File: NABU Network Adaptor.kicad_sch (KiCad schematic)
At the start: 19 parts, among them J1 DIN-5_180degree, J3 RF Module, J5 LEDs, U1 SN74LS164N, U10 UA9638CP, U11 UA9637ATC, U13 SN74LS164N, U19 LM339N, U20 SN74LS164N, U21 SN74LS86N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

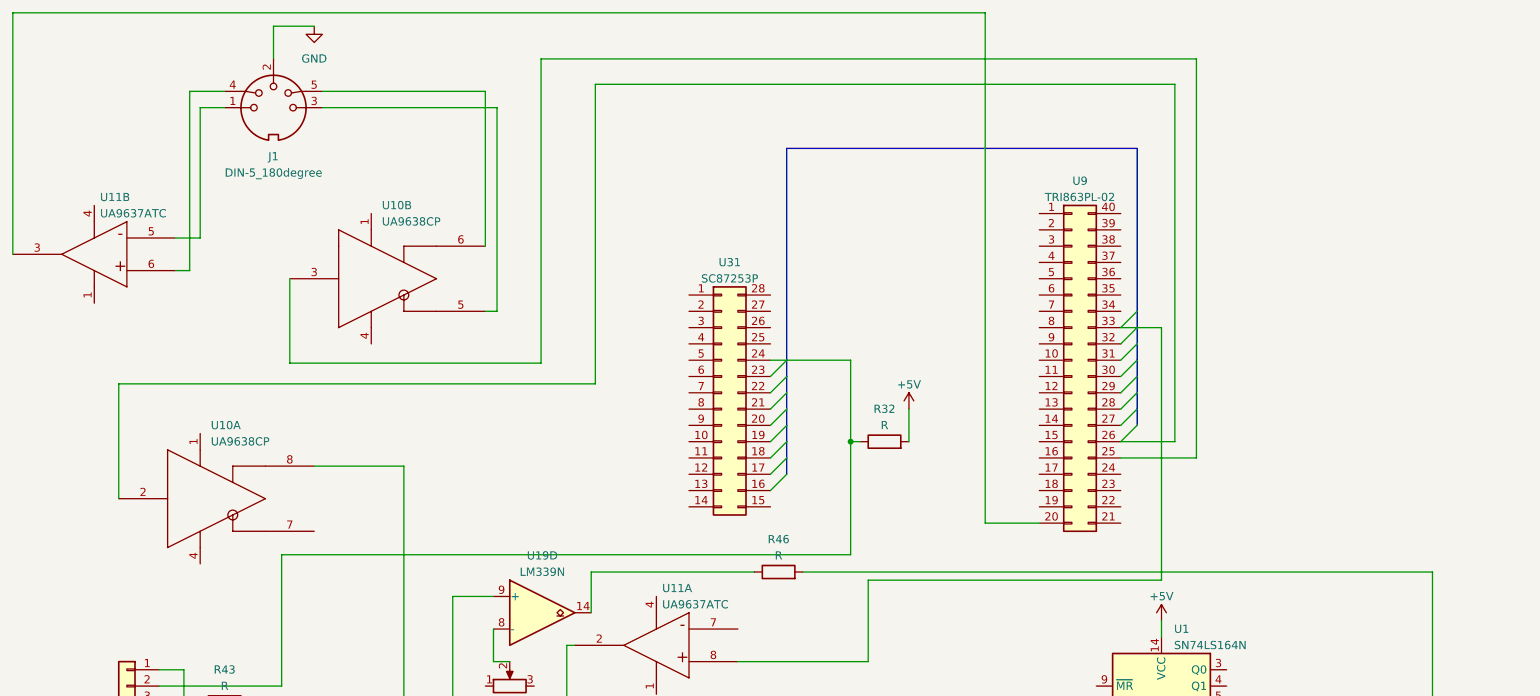
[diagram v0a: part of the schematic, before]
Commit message: Add U8
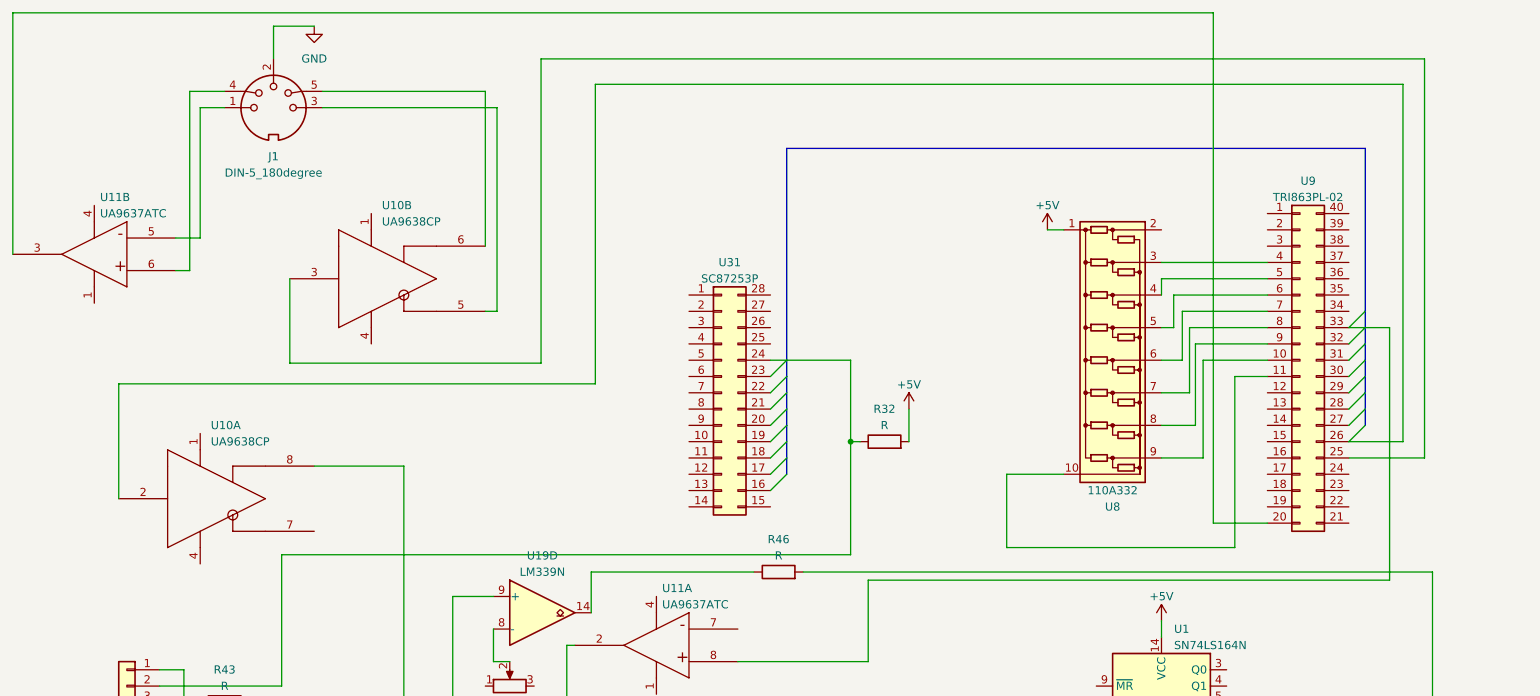
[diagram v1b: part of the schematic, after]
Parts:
- added U8: 110A332, Resistor_THT:R_Array_SIP10, symbol Device:R_Network_Dividers_x08_SIP
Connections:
- net +5V: now also U8.1 (COM1)
- net at U9.10 (Pin_10): now also U8.9 (R8)
- net at U9.11 (Pin_11): now also U8.10 (COM2)
- net at U9.4 (Pin_4): now also U8.3 (R2)
- net at U9.5 (Pin_5): now also U8.4 (R3)
- net at U9.6 (Pin_6): now also U8.5 (R4)
- net at U9.7 (Pin_7): now also U8.6 (R5)
- net at U9.8 (Pin_8): now also U8.7 (R6)
- net at U9.9 (Pin_9): now also U8.8 (R7)
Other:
- moved on the sheet: U9

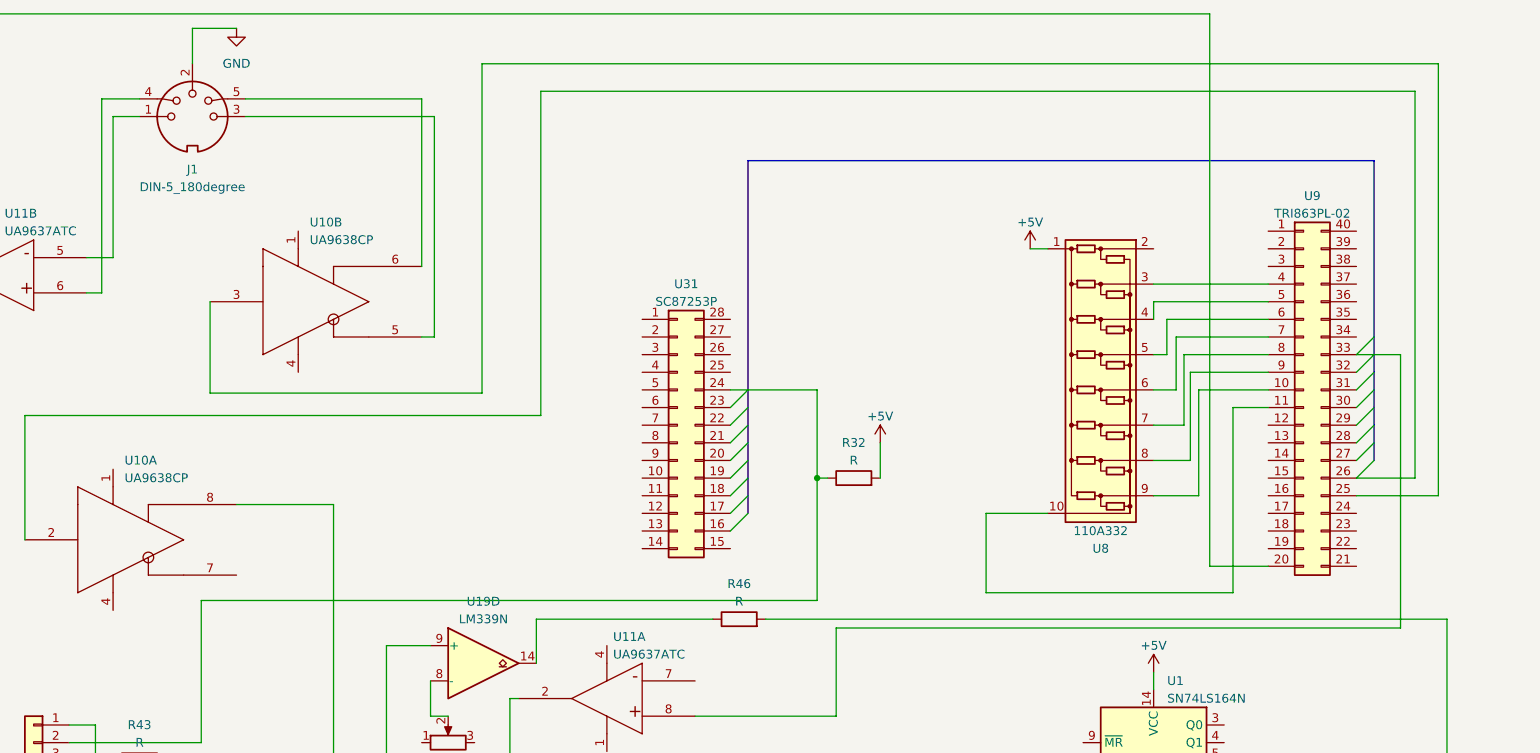
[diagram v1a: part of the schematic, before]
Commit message: Fix U10/U11 to U9 connections
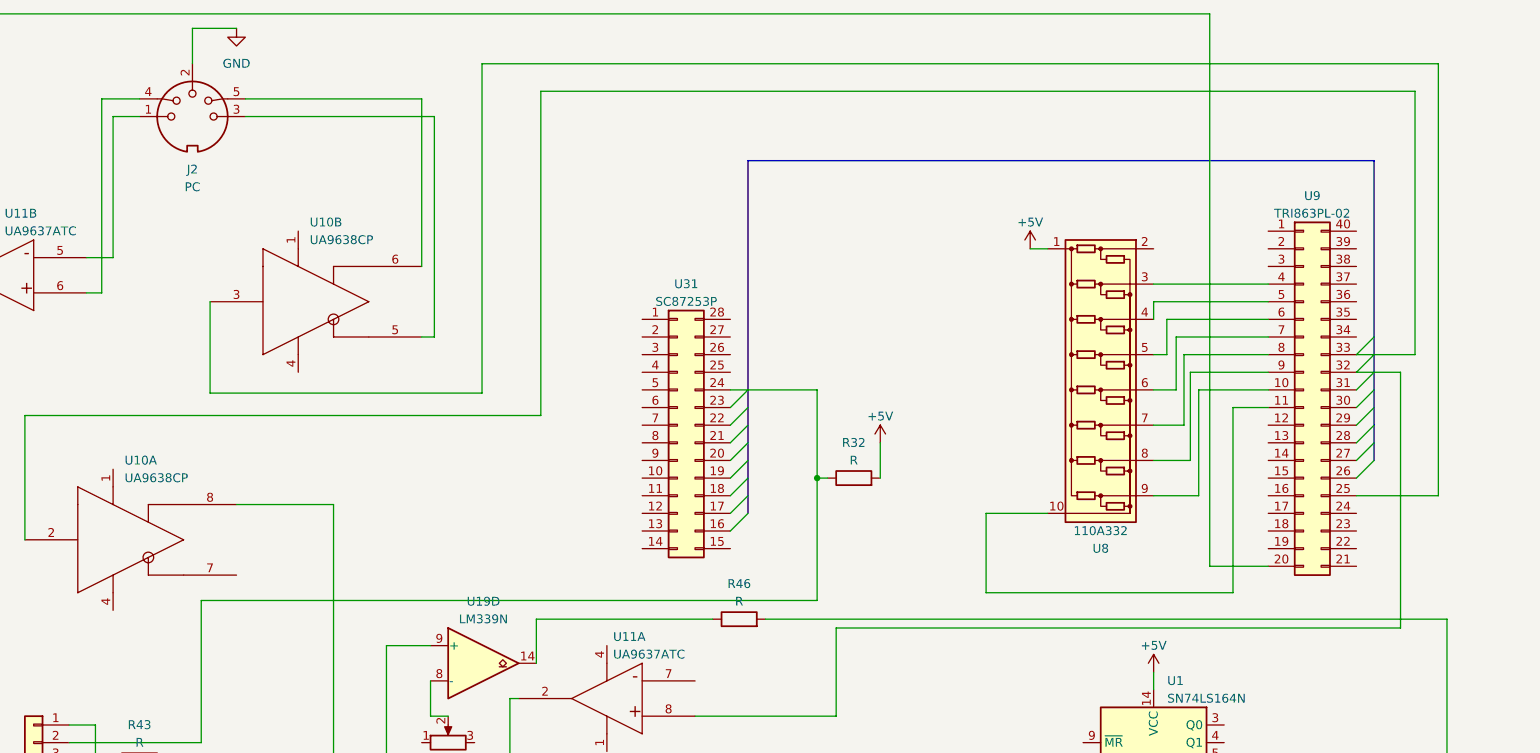
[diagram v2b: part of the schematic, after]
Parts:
- J2: renamed from J1; value DIN-5_180degree -> PC
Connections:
- net at U10.2 (IN): now also U9.33 (Pin_33); no longer U9.26 (Pin_26)
- net at U11.8 (IN+): now also U9.32 (Pin_32); no longer U9.33 (Pin_33)
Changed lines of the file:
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@@
+    (stroke (width 0) (type default))
+  )
+  (wire (pts (xy 231.9554 63.5) (xy 231.9554 25.5713))
     (stroke (width 0) (type default))
   )
@@
     (stroke (width 0) (type default))
   )
-  (wire (pts (xy 226.06 63.5) (xy 229.87 63.5))
-    (stroke (width 0) (type default))
-  )
   (wire (pts (xy 101.6 124.46) (xy 38.1 124.46))
     (stroke (width 0) (type default))
@@
     (stroke (width 0) (type default))
   )
-  (wire (pts (xy 223.52 81.28) (xy 231.9554 81.28))
-    (stroke (width 0) (type default))
-  )
   (wire (pts (xy 101.6 113.03) (xy 102.87 113.03))
     (stroke (width 0) (type default))
@@
     (stroke (width 0) (type default))
   )
+  (wire (pts (xy 226.06 66.04) (xy 223.52 66.04))
+    (stroke (width 0) (type default))
+  )
   (wire (pts (xy 133.35 172.72) (xy 137.16 172.72))
     (stroke (width 0) (type default))
@@
     (stroke (width 0) (type default))
   )
+  (wire (pts (xy 235.3174 83.82) (xy 235.3174 21.6093))
+    (stroke (width 0) (type default))
+  )
+  (wire (pts (xy 194.31 109.22) (xy 194.31 111.76))
+    (stroke (width 0) (type default))
+  )
+  (wire (pts (xy 41.91 116.84) (xy 41.91 129.54))
+    (stroke (width 0) (type default))
+  )
+  (bus (pts (xy 226.06 68.58) (xy 226.06 71.12))
+    (stroke (width 0) (type default))
+  )
+  (wire (pts (xy 106.0506 72.2677) (xy 106.0506 25.5713))
+    (stroke (width 0) (type default))
+  )
+  (wire (pts (xy 236.5593 101.6) (xy 236.5593 158.75))
+    (stroke (width 0) (type default))
+  )
+  (wire (pts (xy 170.18 97.79) (xy 170.18 86.36))
+    (stroke (width 0) (type default))
+  )
+  (wire (pts (xy 106.68 152.4) (xy 128.27 152.4))
+    (stroke (width 0) (type default))
+  )
+  (wire (pts (xy 210.82 63.5) (xy 198.6839 63.5))
+    (stroke (width 0) (type default))
+  )
+  (wire (pts (xy 210.82 55.88) (xy 194.31 55.88))
+    (stroke (width 0) (type default))
+  )
+  (wire (pts (xy 166.37 148.59) (xy 168.3459 148.59))
+    (stroke (width 0) (type default))
+  )
+  (wire (pts (xy 235.3174 21.6093) (xy 97.5862 21.6093))
+    (stroke (width 0) (type default))
+  )
+  (wire (pts (xy 62.23 85.09) (xy 76.2 85.09))
+    (stroke (width 0) (type default))
+  )
+  (bus (pts (xy 226.06 76.2) (xy 226.06 78.74))
+    (stroke (width 0) (type default))
+  )
+  (wire (pts (xy 82.632 160.02) (xy 82.632 165.1))
+    (stroke (width 0) (type default))
+  )
+  (wire (pts (xy 194.31 55.88) (xy 194.31 58.42))
+    (stroke (width 0) (type default))
+  )
+  (wire (pts (xy 144.2154 142.24) (xy 144.2154 151.13))
+    (stroke (width 0) (type default))
+  )
+  (wire (pts (xy 133.35 142.24) (xy 144.2154 142.24))
+    (stroke (width 0) (type default))
+  )
+  (wire (pts (xy 210.82 66.04) (xy 199.6011 66.04))
+    (stroke (width 0) (type default))
+  )
+  (wire (pts (xy 210.82 58.42) (xy 196.2144 58.42))
+    (stroke (width 0) (type default))
+  )
+  (wire (pts (xy 83.82 121.92) (xy 52.07 121.92))
+    (stroke (width 0) (type default))
+  )
+  (wire (pts (xy 179.6351 127) (xy 179.6351 129.54))
+    (stroke (width 0) (type default))
+  )
+  (wire (pts (xy 179.6351 129.54) (xy 173.99 129.54))
+    (stroke (width 0) (type default))
+  )
+  (wire (pts (xy 63.5 29.21) (xy 90.723 29.21))
+    (stroke (width 0) (type default))
+  )
+  (wire (pts (xy 226.06 63.5) (xy 231.9554 63.5))
+    (stroke (width 0) (type default))
+  )
+  (wire (pts (xy 138.43 101.6) (xy 236.5593 101.6))
+    (stroke (width 0) (type default))
+  )
+  (wire (pts (xy 38.1 119.38) (xy 57.15 119.38))
+    (stroke (width 0) (type default))
+  )
+  (wire (pts (xy 229.87 102.87) (xy 229.87 66.04))
+    (stroke (width 0) (type default))
+  )
+  (wire (pts (xy 76.2 144.78) (xy 76.2 147.32))
+    (stroke (width 0) (type default))
+  )
   (wire (pts (xy 223.52 63.5) (xy 226.06 63.5))
     (stroke (width 0) (type default))
   )
-  (wire (pts (xy 229.87 63.5) (xy 229.87 102.87))
-    (stroke (width 0) (type default))
-  )
-  (wire (pts (xy 235.3174 83.82) (xy 235.3174 21.6093))
-    (stroke (width 0) (type default))
-  )
-  (wire (pts (xy 194.31 109.22) (xy 194.31 111.76))
-    (stroke (width 0) (type default))
-  )
-  (wire (pts (xy 41.91 116.84) (xy 41.91 129.54))
-    (stroke (width 0) (type default))
-  )
-  (bus (pts (xy 226.06 68.58) (xy 226.06 71.12))
-    (stroke (width 0) (type default))
-  )
-  (wire (pts (xy 106.0506 72.2677) (xy 106.0506 25.5713))
-    (stroke (width 0) (type default))
-  )
-  (wire (pts (xy 236.5593 101.6) (xy 236.5593 158.75))
-    (stroke (width 0) (type default))
-  )
-  (wire (pts (xy 170.18 97.79) (xy 170.18 86.36))
-    (stroke (width 0) (type default))
-  )
-  (wire (pts (xy 106.68 152.4) (xy 128.27 152.4))
-    (stroke (width 0) (type default))
-  )
-  (wire (pts (xy 210.82 63.5) (xy 198.6839 63.5))
-    (stroke (width 0) (type default))
-  )
-  (wire (pts (xy 210.82 55.88) (xy 194.31 55.88))
-    (stroke (width 0) (type default))
-  )
-  (wire (pts (xy 166.37 148.59) (xy 168.3459 148.59))
-    (stroke (width 0) (type default))
-  )
-  (wire (pts (xy 235.3174 21.6093) (xy 97.5862 21.6093))
-    (stroke (width 0) (type default))
-  )
-  (wire (pts (xy 62.23 85.09) (xy 76.2 85.09))
-    (stroke (width 0) (type default))
-  )
-  (bus (pts (xy 226.06 76.2) (xy 226.06 78.74))
-    (stroke (width 0) (type default))
-  )
-  (wire (pts (xy 82.632 160.02) (xy 82.632 165.1))
-    (stroke (width 0) (type default))
-  )
-  (wire (pts (xy 194.31 55.88) (xy 194.31 58.42))
-    (stroke (width 0) (type default))
-  )
-  (wire (pts (xy 144.2154 142.24) (xy 144.2154 151.13))
-    (stroke (width 0) (type default))
-  )
-  (wire (pts (xy 133.35 142.24) (xy 144.2154 142.24))
-    (stroke (width 0) (type default))
-  )
-  (wire (pts (xy 210.82 66.04) (xy 199.6011 66.04))
-    (stroke (width 0) (type default))
-  )
-  (wire (pts (xy 210.82 58.42) (xy 196.2144 58.42))
-    (stroke (width 0) (type default))
-  )
-  (wire (pts (xy 83.82 121.92) (xy 52.07 121.92))
-    (stroke (width 0) (type default))
-  )
-  (wire (pts (xy 179.6351 127) (xy 179.6351 129.54))
-    (stroke (width 0) (type default))
-  )
-  (wire (pts (xy 179.6351 129.54) (xy 173.99 129.54))
-    (stroke (width 0) (type default))
-  )
-  (wire (pts (xy 63.5 29.21) (xy 90.723 29.21))
-    (stroke (width 0) (type default))
-  )
-  (wire (pts (xy 138.43 101.6) (xy 236.5593 101.6))
-    (stroke (width 0) (type default))
-  )
-  (wire (pts (xy 38.1 119.38) (xy 57.15 119.38))
-    (stroke (width 0) (type default))
-  )
-  (wire (pts (xy 76.2 144.78) (xy 76.2 147.32))
+  (wire (pts (xy 226.06 66.04) (xy 229.87 66.04))
     (stroke (width 0) (type default))
   )
@@
   )
   (wire (pts (xy 41.91 134.62) (xy 41.91 143.51))
-    (stroke (width 0) (type default))
-  )
-  (wire (pts (xy 231.9554 25.5713) (xy 231.9554 81.28))
     (stroke (width 0) (type default))
   )
@@
   (symbol (lib_id "Connector:DIN-5_180degree") (at 55.88 29.21 0) (unit 1)
     (in_bom yes) (on_board yes) (dnp no) (fields_autoplaced)
-    (property "Reference" "J1" (at 55.8801 36.83 0)
-      (effects (font (size 1.27 1.27)))
-    )
-    (property "Value" "DIN-5_180degree" (at 55.8801 39.37 0)
+    (property "Reference" "J2" (at 55.8801 36.83 0)
+      (effects (font (size 1.27 1.27)))
+    )
+    (property "Value" "PC" (at 55.8801 39.37 0)
       (effects (font (size 1.27 1.27)))
     )
@@
       (project "NABU Network Adaptor"
         (path "/fe8087f8-6b92-4d5f-81d9-605adde2f076"
-          (reference "J1") (unit 1)
-        )
-      )
+          (reference "J2") (unit 1)
+        )
+      )
